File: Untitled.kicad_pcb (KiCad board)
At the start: 2 copper layers, 111.8 x 37.5 mm, 20 parts, among them J1 JAMMA, J2 TEST, J3 PLAYER1, J4 PLAYER2, J5 BARREL_JACK, J6 DC-DC, J7 SCART

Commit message: ESP32, shift register and buffer
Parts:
- removed J3: PLAYER1, DSub15Fat:DB15MD
- removed J4: PLAYER2, DSub15Fat:DB15MD
- added C4: 1u, Capacitors_SMD:C_1206_HandSoldering, F.Cu at (136.0, 128.5)
- added U1: LD1117S33TR, TO_SOT_Packages_SMD:SOT-223, B.Cu at (148.0, 130.5)
- added U2: ESP32-WROOM, ESP32-footprints-Lib:ESP32-WROOM, F.Cu at (104.8, 139.6)
- added U3: 74HC595, Housings_SOIC:SOIC-16_3.9x9.9mm_Pitch1.27mm, F.Cu at (131.0, 139.0)
- added U4: 74HC595, Housings_SOIC:SOIC-16_3.9x9.9mm_Pitch1.27mm, F.Cu at (121.0, 139.0)
- added U5: 74HC595, Housings_SOIC:SOIC-16_3.9x9.9mm_Pitch1.27mm, B.Cu at (126.3, 138.9)
- added U6: 74LS06, Housings_SOIC:SOIC-14_3.9x8.7mm_Pitch1.27mm_HandSoldering, F.Cu at (134.5, 149.9)
- added U7: 74LS06, Housings_SOIC:SOIC-14_3.9x8.7mm_Pitch1.27mm_HandSoldering, F.Cu at (121.7, 150.1)
- added U8: 74LS06, Housings_SOIC:SOIC-14_3.9x8.7mm_Pitch1.27mm_HandSoldering, B.Cu at (134.5, 150.0)
- added U9: 74LS06, Housings_SOIC:SOIC-14_3.9x8.7mm_Pitch1.27mm_HandSoldering, B.Cu at (121.7, 149.9)
- C1, C2, C3: value CP -> 4.7u
- J2: value TEST -> CONN_01X06; footprint Buttons_Switches_THT:SW_PUSH_6mm -> Pin_Headers:Pin_Header_Straight_1x06
- J5: value BARREL_JACK -> PWR_IN
- J6: value DC-DC -> DC2DC
- J7: value SCART -> SCART-F
- R1, R2, R3, R4: value R -> 330
- R10: value R -> 100
- R5: value R -> 10K
- R6: value R -> 1K
- R7: value R -> 240
- R8: value R_Variable -> 500
- R9: value R -> 33
- moved J2 31.0 mm to (117.4, 128.5), turned to 90 degrees
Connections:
- J2 pad 1: TEST -> Net-(J2-Pad1)
- J2 pad 2: GND -> Net-(J2-Pad2)
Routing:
- net +5V: track 161.2 -> 266.5 mm, vias 2 -> 8
- net GND: track 310.5 -> 408.2 mm, vias 2 -> 20
- net SERVICE: track 0.00 -> 91.6 mm, vias 0 -> 1
- net TEST: track 14.7 -> 95.4 mm
- net 33: track 0.00 -> 67.2 mm, vias 0 -> 1
- net START1: track 47.1 -> 90.2 mm, vias 1 -> 2
- net Net-(J2-Pad3): track 0.00 -> 41.6 mm, vias 0 -> 1
- net Net-(U4-Pad4): track 0.00 -> 40.5 mm, vias 0 -> 1
- net COIN1: track 51.9 -> 89.6 mm, vias 1 -> 2
- net DATA: track 0.00 -> 37.0 mm
- net Net-(U4-Pad5): track 0.00 -> 36.6 mm, vias 0 -> 1
- net EN: track 0.00 -> 34.0 mm, vias 0 -> 1
- net CLR: track 0.00 -> 30.4 mm, vias 0 -> 3
- net Net-(U4-Pad6): track 0.00 -> 30.2 mm, vias 0 -> 1
- net Net-(U4-Pad7): track 0.00 -> 29.7 mm, vias 0 -> 1
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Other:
- board text removed: "Player 1 Input"
- board text removed: "Player 2 Input"
- board text removed: "Test"

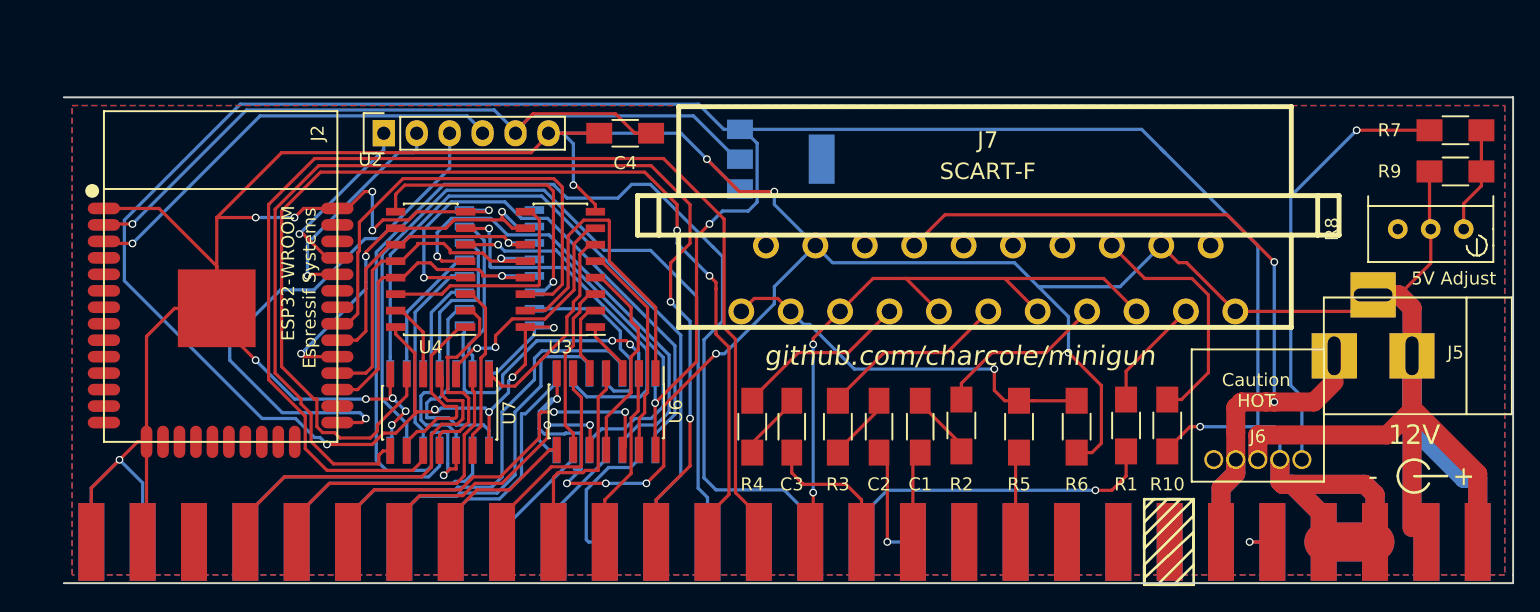
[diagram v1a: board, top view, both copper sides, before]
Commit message: Changed over to NPN transistors as driver
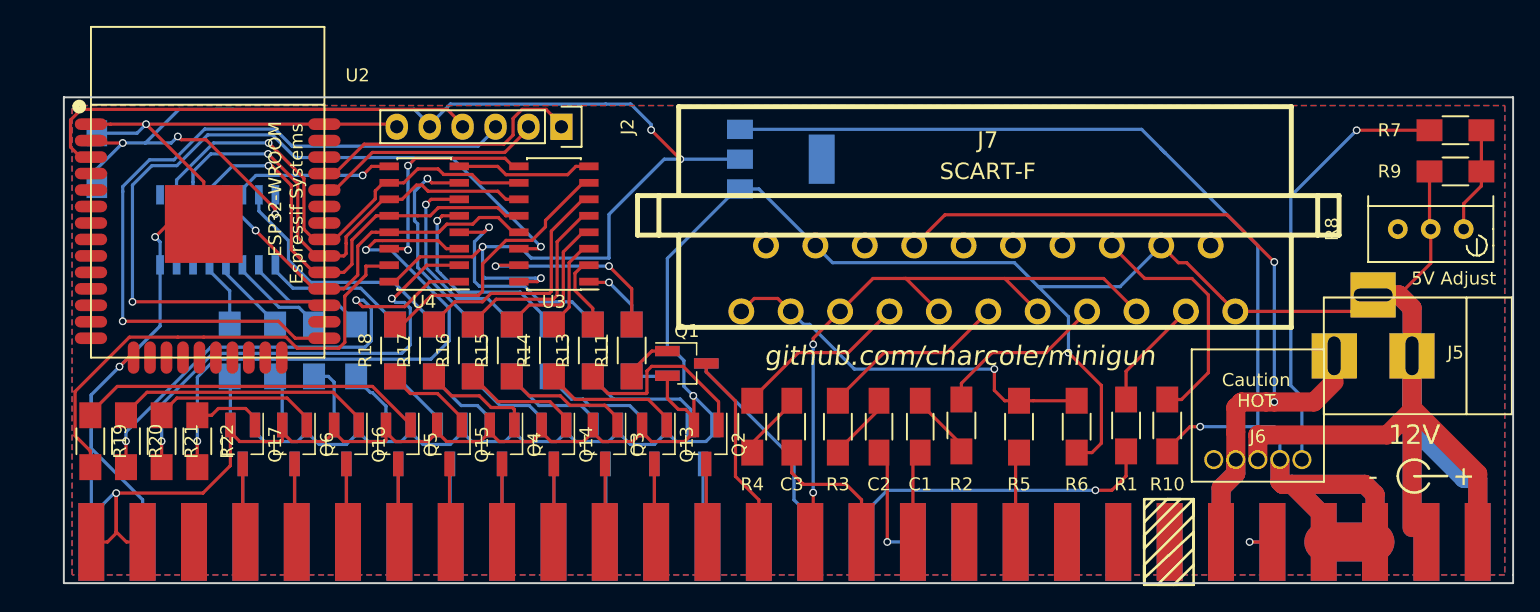
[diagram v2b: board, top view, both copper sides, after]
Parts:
- removed U6, U7, U8, U9: 74LS06, Housings_SOIC:SOIC-14_3.9x8.7mm_Pitch1.27mm_HandSoldering
- added Q1: Q_NPN_BEC, TO_SOT_Packages_SMD:SOT-23_Handsoldering, F.Cu at (140.8, 146.2)
- added Q10: Q_NPN_BEC, TO_SOT_Packages_SMD:SOT-23_Handsoldering, B.Cu at (118.5, 152.5)
- added Q11: Q_NPN_BEC, TO_SOT_Packages_SMD:SOT-23_Handsoldering, B.Cu at (110.5, 152.5)
- added Q12: Q_NPN_BEC, TO_SOT_Packages_SMD:SOT-23_Handsoldering, B.Cu at (140.8, 146.2)
- added Q13: Q_NPN_BEC, TO_SOT_Packages_SMD:SOT-23_Handsoldering, F.Cu at (138.2, 152.5)
- added Q14: Q_NPN_BEC, TO_SOT_Packages_SMD:SOT-23_Handsoldering, F.Cu at (130.5, 152.5)
- added Q15: Q_NPN_BEC, TO_SOT_Packages_SMD:SOT-23_Handsoldering, F.Cu at (122.5, 152.5)
- added Q16: Q_NPN_BEC, TO_SOT_Packages_SMD:SOT-23_Handsoldering, F.Cu at (114.5, 152.5)
- added Q17: Q_NPN_BEC, TO_SOT_Packages_SMD:SOT-23_Handsoldering, F.Cu at (106.5, 152.5)
- added Q18: Q_NPN_BEC, TO_SOT_Packages_SMD:SOT-23_Handsoldering, B.Cu at (138.2, 152.5)
- added Q19: Q_NPN_BEC, TO_SOT_Packages_SMD:SOT-23_Handsoldering, B.Cu at (130.5, 152.5)
- added Q2: Q_NPN_BEC, TO_SOT_Packages_SMD:SOT-23_Handsoldering, F.Cu at (142.2, 152.5)
- added Q20: Q_NPN_BEC, TO_SOT_Packages_SMD:SOT-23_Handsoldering, B.Cu at (122.5, 152.5)
- added Q21: Q_NPN_BEC, TO_SOT_Packages_SMD:SOT-23_Handsoldering, B.Cu at (114.5, 152.5)
- added Q22: Q_NPN_BEC, TO_SOT_Packages_SMD:SOT-23_Handsoldering, B.Cu at (106.5, 152.5)
- added Q3: Q_NPN_BEC, TO_SOT_Packages_SMD:SOT-23_Handsoldering, F.Cu at (134.4, 152.5)
- added Q4: Q_NPN_BEC, TO_SOT_Packages_SMD:SOT-23_Handsoldering, F.Cu at (126.5, 152.5)
- added Q5: Q_NPN_BEC, TO_SOT_Packages_SMD:SOT-23_Handsoldering, F.Cu at (118.5, 152.5)
- added Q6: Q_NPN_BEC, TO_SOT_Packages_SMD:SOT-23_Handsoldering, F.Cu at (110.5, 152.5)
- added Q7: Q_NPN_BEC, TO_SOT_Packages_SMD:SOT-23_Handsoldering, B.Cu at (142.0, 152.5)
- added Q8: Q_NPN_BEC, TO_SOT_Packages_SMD:SOT-23_Handsoldering, B.Cu at (134.5, 152.5)
- added Q9: Q_NPN_BEC, TO_SOT_Packages_SMD:SOT-23_Handsoldering, B.Cu at (126.5, 152.5)
- added R11: R, Resistors_SMD:R_1206_HandSoldering, F.Cu at (136.5, 145.2)
- added R12: R, Resistors_SMD:R_1206_HandSoldering, B.Cu at (136.5, 145.2)
- added R13: R, Resistors_SMD:R_1206_HandSoldering, F.Cu at (133.5, 145.2)
- added R14: R, Resistors_SMD:R_1206_HandSoldering, F.Cu at (130.5, 145.2)
- added R15: R, Resistors_SMD:R_1206_HandSoldering, F.Cu at (127.2, 145.2)
- added R16: R, Resistors_SMD:R_1206_HandSoldering, F.Cu at (124.2, 145.2)
- added R17: R, Resistors_SMD:R_1206_HandSoldering, F.Cu at (121.2, 145.2)
- added R18: R, Resistors_SMD:R_1206_HandSoldering, F.Cu at (118.2, 145.2)
- added R19: R, Resistors_SMD:R_1206_HandSoldering, F.Cu at (94.8, 152.2)
- added R20: R, Resistors_SMD:R_1206_HandSoldering, F.Cu at (97.5, 152.2)
- added R21: R, Resistors_SMD:R_1206_HandSoldering, F.Cu at (100.2, 152.2)
- added R22: R, Resistors_SMD:R_1206_HandSoldering, F.Cu at (103.0, 152.2)
- added R23: R, Resistors_SMD:R_1206_HandSoldering, B.Cu at (133.5, 145.2)
- added R24: R, Resistors_SMD:R_1206_HandSoldering, B.Cu at (130.2, 145.2)
- added R25: R, Resistors_SMD:R_1206_HandSoldering, B.Cu at (127.2, 145.2)
- added R26: R, Resistors_SMD:R_1206_HandSoldering, B.Cu at (124.2, 145.2)
- added R27: R, Resistors_SMD:R_1206_HandSoldering, B.Cu at (121.2, 145.2)
- added R28: R, Resistors_SMD:R_1206_HandSoldering, B.Cu at (118.2, 145.2)
- added R29: R, Resistors_SMD:R_1206_HandSoldering, B.Cu at (115.2, 145.2)
- added R30: R, Resistors_SMD:R_1206_HandSoldering, B.Cu at (112.0, 145.2)
- added R31: R, Resistors_SMD:R_1206_HandSoldering, B.Cu at (109.0, 145.2)
- added R32: R, Resistors_SMD:R_1206_HandSoldering, B.Cu at (105.5, 145.2)
- C4: moved to B.Cu
- moved C4 40.8 mm to (95.2, 130.5), turned to 90 degrees
- moved U5 21.9 mm to (104.6, 135.9), turned to 90 degrees
- moved J2 13.7 mm to (131.1, 128.0), turned to 270 degrees
- moved U2 6.58 mm to (103.8, 133.1)
- moved U3 3.54 mm to (130.5, 135.5)
- moved U4 3.54 mm to (120.5, 135.5)
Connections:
- J1 pad 13: Net-(J1-Pad13) -> (no net)
- J1 pad 14: Net-(J1-Pad14) -> (no net)
- J1 pad 15: Net-(J1-Pad15) -> (no net)
- J1 pad 16: Net-(J1-Pad16) -> (no net)
- J1 pad 17: Net-(J1-Pad17) -> (no net)
- J1 pad 18: Net-(J1-Pad18) -> (no net)
- J1 pad 20: Net-(J1-Pad20) -> (no net)
- J1 pad 21: Net-(J1-Pad21) -> (no net)
- J1 pad 22: Net-(J1-Pad22) -> (no net)
- J1 pad 30: Net-(J1-Pad30) -> (no net)
- J1 pad 51: Net-(J1-Pad51) -> (no net)
- J1 pad 52: Net-(J1-Pad52) -> (no net)
- J6 pad 1: Net-(J6-Pad1) -> (no net)
- J7 pad 10: Net-(J7-Pad10) -> (no net)
- J7 pad 12: Net-(J7-Pad12) -> (no net)
- J7 pad 14: Net-(J7-Pad14) -> (no net)
- J7 pad 2: Net-(J7-Pad2) -> (no net)
- J7 pad 20: Net-(J7-Pad20) -> (no net)
- J7 pad 6: Net-(J7-Pad6) -> (no net)
- U2 pad 10: Net-(U2-Pad10) -> (no net)
- U2 pad 11: Net-(U2-Pad11) -> (no net)
- U2 pad 12: Net-(U2-Pad12) -> (no net)
- U2 pad 13: Net-(U2-Pad13) -> (no net)
- U2 pad 14: Net-(U2-Pad14) -> (no net)
- U2 pad 16: Net-(U2-Pad16) -> (no net)
- U2 pad 17: Net-(U2-Pad17) -> (no net)
- U2 pad 18: Net-(U2-Pad18) -> (no net)
- U2 pad 19: Net-(U2-Pad19) -> (no net)
- U2 pad 20: Net-(U2-Pad20) -> (no net)
- U2 pad 21: Net-(U2-Pad21) -> (no net)
- U2 pad 22: Net-(U2-Pad22) -> (no net)
- U2 pad 23: Net-(U2-Pad23) -> (no net)
- U2 pad 24: Net-(U2-Pad24) -> (no net)
- U2 pad 26: Net-(U2-Pad26) -> (no net)
- U2 pad 27: OE -> DATA
- U2 pad 28: LATCH -> OE
- U2 pad 29: CLR -> LATCH
- U2 pad 31: DATA -> CLR
- U2 pad 32: Net-(U2-Pad32) -> (no net)
- U2 pad 33: Net-(U2-Pad33) -> (no net)
- U2 pad 36: Net-(U2-Pad36) -> (no net)
- U2 pad 37: Net-(U2-Pad37) -> (no net)
- U2 pad 4: Net-(U2-Pad4) -> (no net)
- U2 pad 5: Net-(U2-Pad5) -> (no net)
- U2 pad 6: Net-(U2-Pad6) -> (no net)
- U2 pad 7: Net-(U2-Pad7) -> (no net)
- U2 pad 8: Net-(U2-Pad8) -> (no net)
- U2 pad 9: Net-(U2-Pad9) -> (no net)
- U3 pad 16: +5V -> 33
- U4 pad 16: +5V -> 33
- U5 pad 16: +5V -> 33
- U5 pad 6: Net-(U5-Pad6) -> (no net)
- U5 pad 7: Net-(U5-Pad7) -> (no net)
- U5 pad 9: Net-(U5-Pad9) -> (no net)
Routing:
- net +5V: track 266.5 -> 115.2 mm, vias 8 -> 1
- net START1: track 90.2 -> 6.08 mm, vias 2 -> 0
- net COIN1: track 89.6 -> 6.06 mm, vias 2 -> 0
- net TEST: track 95.4 -> 17.4 mm
- net SERVICE: track 91.6 -> 17.1 mm, vias 1 -> 0
- net COIN2: track 64.8 -> 6.16 mm
- net START2: track 54.6 -> 6.08 mm
- net 33: track 67.2 -> 112.3 mm, vias 1 -> 7
- net Net-(R22-Pad2): track 13.4 -> 46.1 mm, vias 0 -> 2
- net Net-(R19-Pad2): track 6.07 -> 37.8 mm
- net B2: track 33.5 -> 6.07 mm
- net DATA: track 37.0 -> 64.0 mm, vias 0 -> 2
- net Net-(Q5-Pad1): track 0.00 -> 27.0 mm
- net B1: track 31.4 -> 6.07 mm, vias 2 -> 0
- net Net-(R23-Pad2): track 40.5 -> 17.7 mm
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
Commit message: Simplied version using LED driver chips
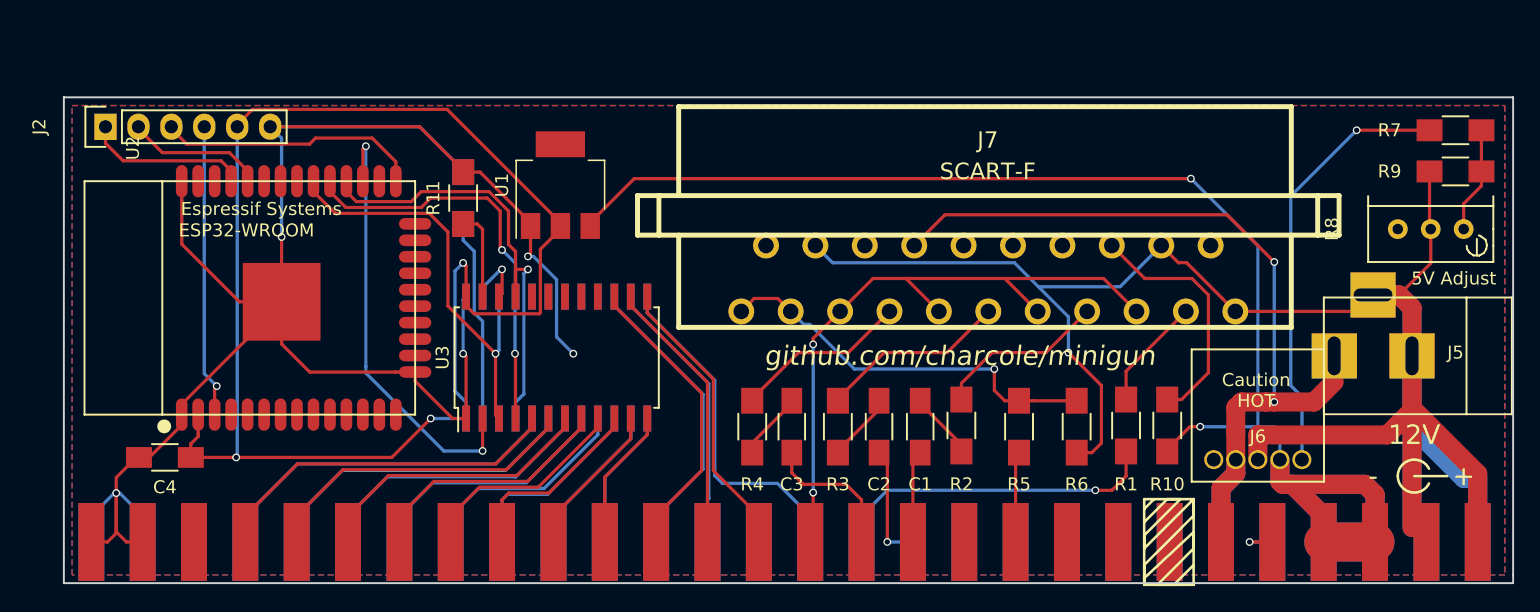
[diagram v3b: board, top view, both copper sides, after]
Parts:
- removed Q1, Q10, Q11, Q12, Q13, Q14, Q15, Q16, Q17, Q18, Q19, Q2, Q20, Q21, Q22, Q3, Q4, Q5, Q6, Q7, Q8, Q9: Q_NPN_BEC, TO_SOT_Packages_SMD:SOT-23_Handsoldering
- removed R13, R14, R15, R16, R17, R18, R19, R20, R21, R22, R23, R24, R25, R26, R27, R28, R29, R30, R31, R32: R, Resistors_SMD:R_1206_HandSoldering
- removed U5: 74HC595, Housings_SOIC:SOIC-16_3.9x9.9mm_Pitch1.27mm
- C4, U1: moved to F.Cu
- U3: value 74HC595 -> TLC5926IDW; footprint Housings_SOIC:SOIC-16_3.9x9.9mm_Pitch1.27mm -> Housings_SOIC:SOIC-24W_7.5x15.4mm_Pitch1.27mm
- U4: value 74HC595 -> TLC5926IDW; footprint Housings_SOIC:SOIC-16_3.9x9.9mm_Pitch1.27mm -> Housings_SOIC:SOIC-24W_7.5x15.4mm_Pitch1.27mm; moved to B.Cu
- moved J2 35.2 mm to (95.9, 128.0), turned to 90 degrees
- moved C4 23.6 mm to (100.5, 153.5), turned to 180 degrees
- moved R11 17.5 mm to (123.5, 133.5)
- moved R12 17.5 mm to (123.5, 133.5)
- moved U1 17.1 mm to (131.0, 132.5), turned to 90 degrees
- moved U4 14.5 mm to (130.7, 145.8), turned to 270 degrees
- moved U3 10.3 mm to (130.7, 145.8), turned to 90 degrees
- moved U2 8.77 mm to (107.0, 141.2), turned to 270 degrees
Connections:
- R11 pad 1: Net-(Q1-Pad1) -> Net-(R11-Pad1)
- R11 pad 2: Net-(R11-Pad2) -> GND
- R12 pad 1: Net-(Q12-Pad1) -> Net-(R12-Pad1)
- R12 pad 2: Net-(R12-Pad2) -> GND
- U2 pad 31: CLR -> (no net)
- U3 pad 1: Net-(R12-Pad2) -> GND
- U3 pad 10: CLR -> LEFT1
- U3 pad 11: CLK -> DOWN1
- U3 pad 12: LATCH -> UP1
- U3 pad 13: OE -> TEST
- U3 pad 14: DATA -> COIN1
- U3 pad 15: Net-(R11-Pad2) -> START1
- U3 pad 16: 33 -> (no net)
- U3 pad 2: Net-(R13-Pad2) -> DATA
- U3 pad 3: Net-(R14-Pad2) -> CLK
- U3 pad 4: Net-(R15-Pad2) -> LATCH
- U3 pad 5: Net-(R16-Pad2) -> D1
- U3 pad 6: Net-(R17-Pad2) -> C1
- U3 pad 7: Net-(R18-Pad2) -> B1
- U3 pad 8: GND -> A1
- U3 pad 9: Net-(U3-Pad9) -> RIGHT1
- U4 pad 1: Net-(R20-Pad2) -> GND
- U4 pad 10: CLR -> START2
- U4 pad 11: CLK -> COIN2
- U4 pad 12: LATCH -> SERVICE
- U4 pad 13: OE -> UP2
- U4 pad 14: Net-(U3-Pad9) -> DOWN2
- U4 pad 15: Net-(R19-Pad2) -> LEFT2
- U4 pad 16: 33 -> RIGHT2
- U4 pad 2: Net-(R21-Pad2) -> Net-(U3-Pad22)
- U4 pad 3: Net-(R22-Pad2) -> CLK
- U4 pad 4: Net-(R23-Pad2) -> LATCH
- U4 pad 5: Net-(R24-Pad2) -> (no net)
- U4 pad 6: Net-(R25-Pad2) -> (no net)
- U4 pad 7: Net-(R26-Pad2) -> (no net)
- U4 pad 8: GND -> (no net)
- U4 pad 9: Net-(U4-Pad9) -> (no net)
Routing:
- net GND: track 424.4 -> 321.6 mm
- net Net-(R22-Pad2): track 46.1 -> 0.00 mm, vias 2 -> 0
- net Net-(J2-Pad3): track 58.3 -> 20.4 mm, vias 1 -> 0
- net Net-(R19-Pad2): track 37.8 -> 0.00 mm
- net Net-(R20-Pad2): track 37.5 -> 0.00 mm, vias 2 -> 0
- net CLR: track 37.2 -> 0.00 mm, vias 1 -> 0
- net Net-(R21-Pad2): track 36.7 -> 0.00 mm, vias 2 -> 0
- net DATA: track 64.0 -> 34.3 mm
- net Net-(Q5-Pad1): track 27.0 -> 0.00 mm
- net D2: track 6.10 -> 27.6 mm
- net D1: track 6.10 -> 27.6 mm
- net Net-(R18-Pad2): track 21.0 -> 0.00 mm
- net Net-(Q16-Pad1): track 20.1 -> 0.00 mm
- net Net-(R27-Pad2): track 19.3 -> 0.00 mm
- net C1: track 6.09 -> 24.9 mm
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
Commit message: Added reset/upload buttons
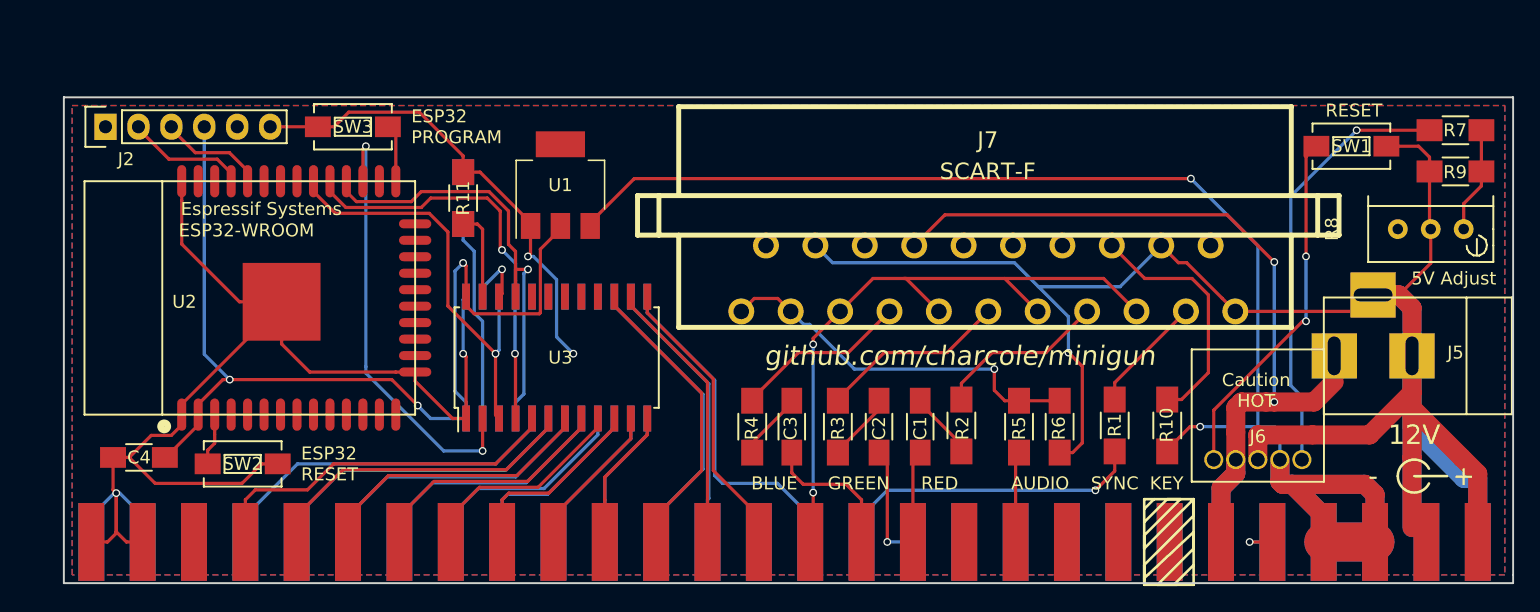
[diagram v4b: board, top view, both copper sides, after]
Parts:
- added SW1: SW_Push, Buttons_Switches_SMD:SW_SPST_EVQPE1, F.Cu at (192.0, 129.5)
- added SW2: SW_Push, Buttons_Switches_SMD:SW_SPST_EVQPE1, F.Cu at (106.5, 154.0)
- added SW3: SW_Push, Buttons_Switches_SMD:SW_SPST_EVQPE1, F.Cu at (115.0, 128.0)
- moved C4 2.00 mm to (98.5, 153.5)
- moved R6 1.31 mm to (169.5, 151.1)
- moved R1 0.88 mm to (173.8, 151.0)
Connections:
- J2 pad 1: Net-(J2-Pad1) -> (no net)
- J2 pad 4: EN -> 33
- J2 pad 5: 33 -> (no net)
- J6 pad 1: (no net) -> Net-(J6-Pad1)
- U2 pad 25: Net-(J2-Pad3) -> Net-(SW3-Pad1)
- U2 pad 3: EN -> Net-(SW2-Pad2)
- U2 pad 34: Net-(J2-Pad2) -> Net-(J2-Pad3)
- U2 pad 35: Net-(J2-Pad1) -> Net-(J2-Pad2)
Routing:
- net 33: track 110.3 -> 77.8 mm
- net Net-(J6-Pad1): track 0.00 -> 27.6 mm, vias 0 -> 2
- net EN: track 22.7 -> 0.00 mm, vias 1 -> 0
- net Net-(J2-Pad1): track 12.6 -> 0.00 mm
- net Net-(J2-Pad3): track 20.4 -> 8.18 mm
- net GND: track 321.6 -> 312.1 mm, vias 6 -> 5
- net Net-(SW3-Pad1): track 0.00 -> 4.45 mm
- net Net-(SW2-Pad2): track 0.00 -> 4.02 mm
- net Net-(J7-Pad1): track 30.5 -> 29.2 mm
- net SYNC: track 25.6 -> 24.5 mm
- net D1: track 27.6 -> 28.4 mm
- net Net-(J2-Pad2): track 10.7 -> 10.1 mm
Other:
- board text added: "AUDIO"
- board text added: "BLUE"
- board text added: "ESP32 PROGRAM"
- board text added: "ESP32 RESET"
- board text added: "GREEN"
- board text added: "KEY"
- board text added: "RED"
- board text added: "RESET"
- board text added: "SYNC"
